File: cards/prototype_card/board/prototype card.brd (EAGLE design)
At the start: 100 x 80 mm, 22 parts, among them J1 09231486921, J2 TBP02R1-381-14BE

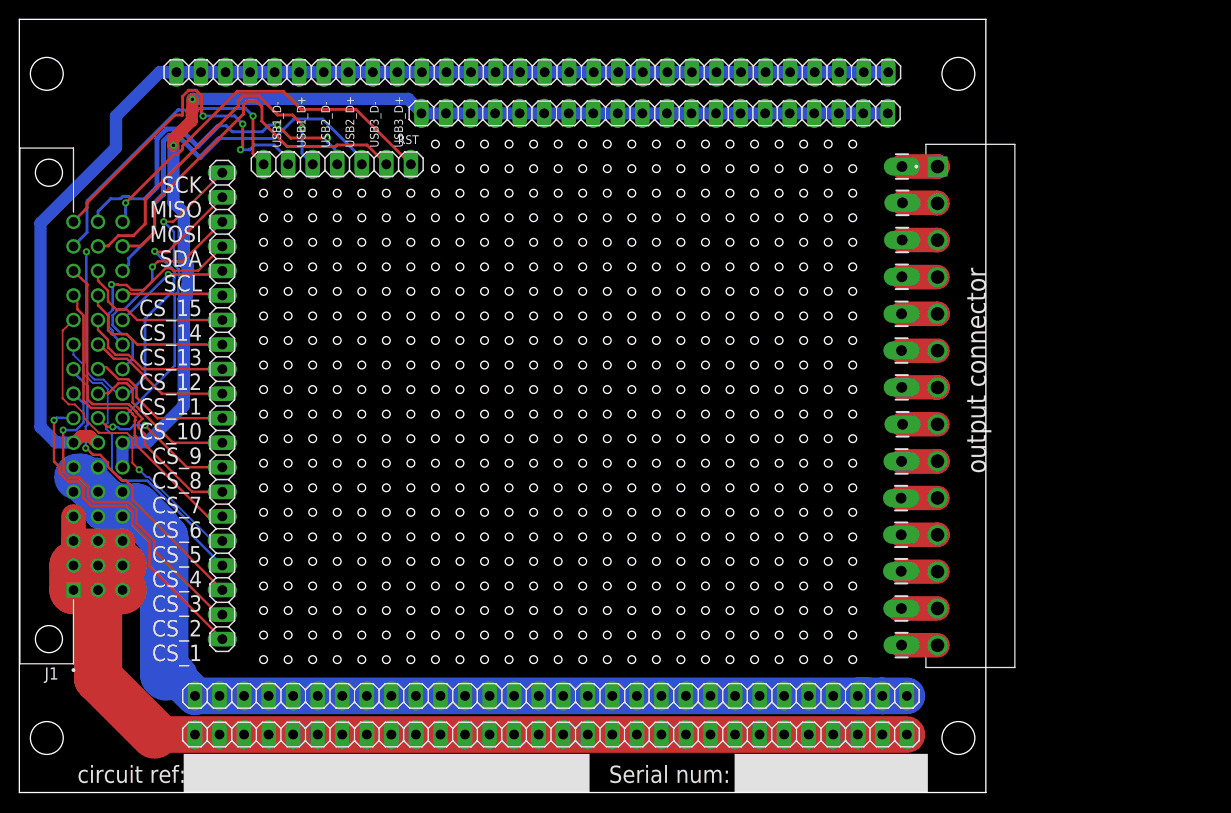
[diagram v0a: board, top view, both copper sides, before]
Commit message: fixed problems with control module 2.2, all boards are now ready to order
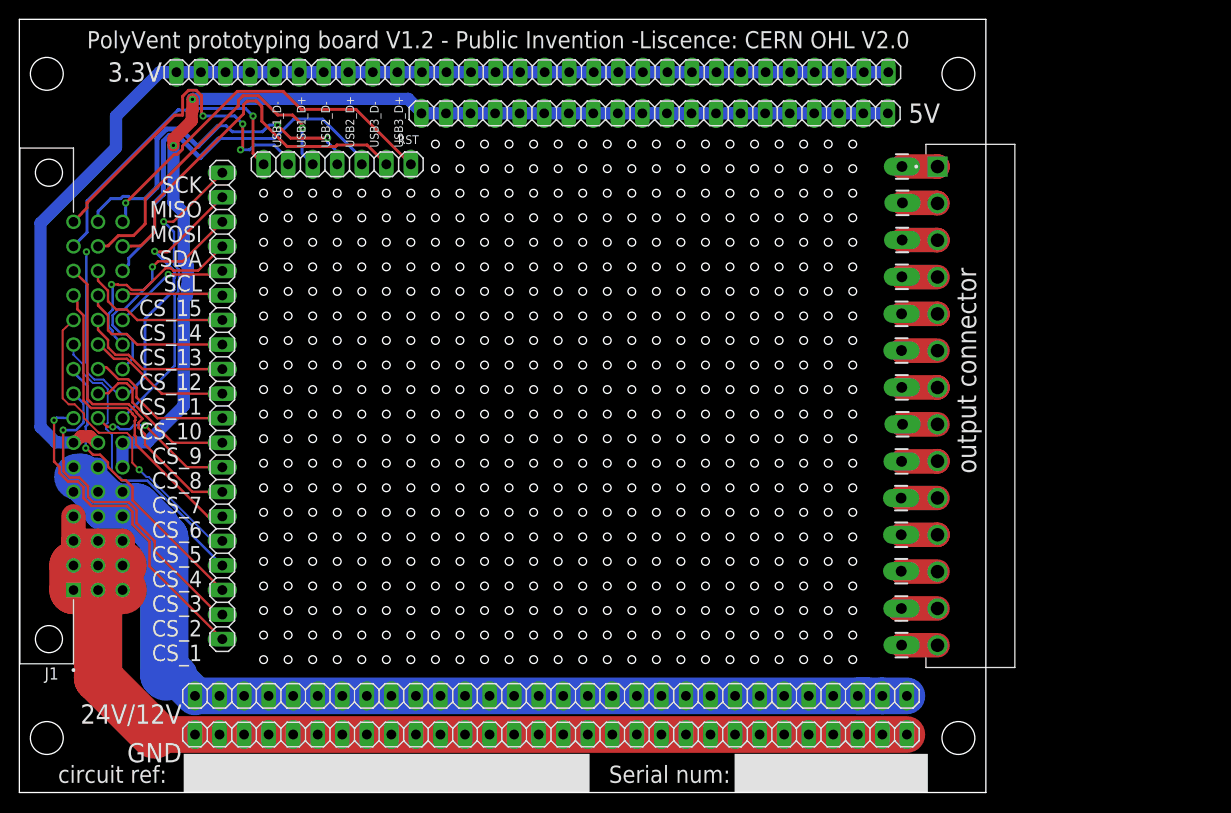
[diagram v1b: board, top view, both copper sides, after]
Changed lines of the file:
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@@
 <drawing>
 <settings>
-<setting alwaysvectorfont="no"/>
+<setting alwaysvectorfont="yes"/>
 <setting verticaltext="up"/>
 </settings>
@@
 CS_1
 </text>
-<hole x="25.27" y="13.75" drill="0.8" grouprefs="PAD 22_PADS"/>
-<rectangle x1="24.27" y1="12.75" x2="26.27" y2="14.75" layer="17" grouprefs="PAD 22_PADS"/>
+<hole x="25.27" y="13.75" drill="0.8" grouprefs="22_PADS PAD"/>
+<rectangle x1="24.27" y1="12.75" x2="26.27" y2="14.75" layer="17" grouprefs="22_PADS PAD"/>
 <hole x="27.81" y="13.75" drill="0.8" grouprefs="22_PADS"/>
 <hole x="30.35" y="13.75" drill="0.8" grouprefs="22_PADS"/>
@@
 <rectangle x1="80.15" y1="66.09" x2="82.15" y2="68.09" layer="17"/>
 <rectangle x1="82.69" y1="66.09" x2="84.69" y2="68.09" layer="17"/>
-<text x="100" y="33" size="2" layer="25" rot="R90">output connector</text>
+<text x="99" y="33" size="2" layer="25" rot="R90">output connector</text>
 <rectangle x1="24" y1="12" x2="87.49" y2="63.4" layer="30"/>
 <rectangle x1="24" y1="12" x2="87.49" y2="63.4" layer="29"/>
-<text x="7" y="77" size="1.778" layer="29">PolyVent prototyping board V1.2 - Public Invention -Liscence: CERN OHL V2.0</text>
-<text x="16.81" y="3.12" size="2" layer="29" distance="0" align="bottom-right">24V/12V
+<text x="7" y="77" size="1.778" layer="25">PolyVent prototyping board V1.2 - Public Invention -Liscence: CERN OHL V2.0</text>
+<text x="16.81" y="3.12" size="2" layer="25" distance="0" align="bottom-right">24V/12V
 GND
 </text>
 <rectangle x1="17" y1="0" x2="59" y2="4" layer="25"/>
-<text x="6" y="1" size="1.778" layer="25">circuit ref: </text>
+<text x="4" y="1" size="1.778" layer="25">circuit ref: </text>
 <text x="61" y="1" size="1.778" layer="25">Serial num:</text>
 <rectangle x1="74" y1="0" x2="94" y2="4" layer="25"/>
 <rectangle x1="42" y1="63.29" x2="87.5" y2="68.42" layer="29"/>
 <rectangle x1="42" y1="63.28" x2="87.48" y2="68.47" layer="30"/>
-<text x="14.76" y="73.55" size="2" layer="29" distance="0" align="bottom-right">3.3V</text>
-<text x="95.26" y="69.29" size="2" layer="29" distance="0" align="bottom-right">5V</text>
+<text x="14.76" y="73.55" size="2" layer="25" distance="0" align="bottom-right">3.3V</text>
+<text x="95.26" y="69.29" size="2" layer="25" distance="0" align="bottom-right">5V</text>
 <text x="42.21" y="66.73" size="0.9" layer="25" distance="40" rot="R90">USB1_D-
 USB1_D+
